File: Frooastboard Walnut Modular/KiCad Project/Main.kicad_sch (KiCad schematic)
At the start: 214 parts, among them J10 F Row CS, J11 F Row SW, J15 F Row, J16 F Row USB, J17 Numpad, J8 Numpad CS, J9 Numpad SW, M2 Frooastboard_MM2040

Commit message: some stuff and caps lock
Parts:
- added MX22: Caps Lock, MX_Only:MXOnly-1U-NoLED, symbol MX_Alps_Hybrid:MX-NoLED
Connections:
- net COL0: now also MX22.1 (COL)
- net at D115.2 (A), MX41.2 (ROW): now also MX22.2 (ROW)
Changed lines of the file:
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@@
   (junction (at 223.52 72.39) (diameter 0) (color 0 0 0 0)
   )
+  (junction (at 58.42 222.25) (diameter 0) (color 0 0 0 0)
+  )
   (junction (at 172.72 195.58) (diameter 0) (color 0 0 0 0)
   )
@@
   (junction (at 256.54 40.64) (diameter 0) (color 0 0 0 0)
   )
+  (junction (at 63.5 217.17) (diameter 0) (color 0 0 0 0)
+  )
   (junction (at 63.5 54.61) (diameter 0) (color 0 0 0 0)
   )
@@
         )
       )
+    )
+  )
+  (symbol (lib_id "MX_Alps_Hybrid:MX-NoLED") (at 59.69 218.44 0) (unit 1)
+    (in_bom yes) (on_board yes) (dnp no) (fields_autoplaced)
+    (property "Reference" "MX22" (at 60.5756 212.09 0)
+      (effects (font (size 1.524 1.524)))
+    )
+    (property "Value" "Caps Lock" (at 60.5756 213.36 0)
+      (effects (font (size 0.508 0.508)))
+    )
+    (property "Footprint" "MX_Only:MXOnly-1U-NoLED" (at 43.815 219.075 0)
+      (effects (font (size 1.524 1.524)) hide)
+    )
+    (property "Datasheet" "" (at 43.815 219.075 0)
+      (effects (font (size 1.524 1.524)) hide)
+    )
+    (pin "1")
+    (pin "2")
+    (instances
+      (project "Frooastboard Walnut Modular"
+        (path "/e63e39d7-6ac0-4ffd-8aa3-1841a4541b55/da496a6d-9c73-4726-8a69-2d6a4df38c58"
+          (reference "MX22") (unit 1)
+        )
+      )

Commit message: stuff
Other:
- moved on the sheet: MX42
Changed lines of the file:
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@@
   (junction (at 177.8 54.61) (diameter 0) (color 0 0 0 0)
   )
-  (junction (at 58.42 238.76) (diameter 0) (color 0 0 0 0)
-  )
   (junction (at 325.12 58.42) (diameter 0) (color 0 0 0 0)
   )
@@
   (junction (at 119.38 58.42) (diameter 0) (color 0 0 0 0)
   )
-  (junction (at 63.5 233.68) (diameter 0) (color 0 0 0 0)
-  )
   (junction (at 162.56 231.14) (diameter 0) (color 0 0 0 0)
   )
@@
   (junction (at 38.1 91.44) (diameter 0) (color 0 0 0 0)
   )
+  (junction (at 58.42 238.76) (diameter 0) (color 0 0 0 0)
+  )
   (junction (at 267.97 138.43) (diameter 0) (color 0 0 0 0)
   )
@@
   (junction (at 335.28 55.88) (diameter 0) (color 0 0 0 0)
   )
+  (junction (at 63.5 233.68) (diameter 0) (color 0 0 0 0)
+  )
   (junction (at 309.88 36.83) (diameter 0) (color 0 0 0 0)
   )
@@
     (stroke (width 0) (type default))
   )
+  (wire (pts (xy 63.5 232.41) (xy 63.5 233.68))
+    (stroke (width 0) (type default))
+  )
   (wire (pts (xy 292.1 72.39) (xy 287.02 72.39))
     (stroke (width 0) (type default))
@@
     (stroke (width 0) (type default))
   )
+  (wire (pts (xy 57.15 238.76) (xy 58.42 238.76))
+    (stroke (width 0) (type default))
+  )
   (wire (pts (xy 25.4 58.42) (xy 50.8 58.42))
     (stroke (width 0) (type default))
@@
     (stroke (width 0) (type default))
   )
+  (wire (pts (xy 62.23 232.41) (xy 63.5 232.41))
+    (stroke (width 0) (type default))
+  )
   (wire (pts (xy 124.46 78.74) (xy 147.32 78.74))
     (stroke (width 0) (type default))
@@
     (stroke (width 0) (type default))
   )
+  (wire (pts (xy 57.15 237.49) (xy 57.15 238.76))
+    (stroke (width 0) (type default))
+  )
   (wire (pts (xy 396.24 173.99) (xy 396.24 176.53))
     (stroke (width 0) (type default))
@@
     )
   )
-  (symbol (lib_id "MX_Alps_Hybrid:MX-NoLED") (at 59.69 234.95 0) (unit 1)
+  (symbol (lib_id "MX_Alps_Hybrid:MX-NoLED") (at 58.42 233.68 0) (unit 1)
     (in_bom yes) (on_board yes) (dnp no) (fields_autoplaced)
-    (property "Reference" "MX42" (at 60.5756 228.6 0)
+    (property "Reference" "MX42" (at 59.3056 227.33 0)
       (effects (font (size 1.524 1.524)))
     )
-    (property "Value" "Left Shift" (at 60.5756 229.87 0)
+    (property "Value" "Left Shift" (at 59.3056 228.6 0)
       (effects (font (size 0.508 0.508)))
     )
-    (property "Footprint" "MX_Only:MXOnly-1.25U-NoLED" (at 43.815 235.585 0)
+    (property "Footprint" "MX_Only:MXOnly-1.25U-NoLED" (at 42.545 234.315 0)
       (effects (font (size 1.524 1.524)) hide)
     )
-    (property "Datasheet" "" (at 43.815 235.585 0)
+    (property "Datasheet" "" (at 42.545 234.315 0)
       (effects (font (size 1.524 1.524)) hide)
     )

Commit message: all keys placed
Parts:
- added MX114: Super Delete, MX_Only:MXOnly-1U-NoLED, symbol MX_Alps_Hybrid:MX-NoLED
- added MX115: End, MX_Only:MXOnly-1U-NoLED, symbol MX_Alps_Hybrid:MX-NoLED
- added MX116: Home, MX_Only:MXOnly-1U-NoLED, symbol MX_Alps_Hybrid:MX-NoLED
- added MX117: Right Control, MX_Only:MXOnly-1U-NoLED, symbol MX_Alps_Hybrid:MX-NoLED
- added MX118: Menu, MX_Only:MXOnly-1U-NoLED, symbol MX_Alps_Hybrid:MX-NoLED
- added MX119: Right Alt, MX_Only:MXOnly-1U-NoLED, symbol MX_Alps_Hybrid:MX-NoLED
- added MX120: Function, MX_Only:MXOnly-1U-NoLED, symbol MX_Alps_Hybrid:MX-NoLED
- added MX121: Shifted Function, MX_Only:MXOnly-1U-NoLED, symbol MX_Alps_Hybrid:MX-NoLED
- added MX122: Space TS, MX_Only:MXOnly-7U-ReversedStabilizers-NoLED, symbol MX_Alps_Hybrid:MX-NoLED
- added MX123: Left Control TS, MX_Only:MXOnly-1.5U-NoLED, symbol MX_Alps_Hybrid:MX-NoLED
- added MX124: Left GUI TS, MX_Only:MXOnly-1U-NoLED, symbol MX_Alps_Hybrid:MX-NoLED
- added MX125: Left Alt TS, MX_Only:MXOnly-1.5U-NoLED, symbol MX_Alps_Hybrid:MX-NoLED
- added MX126: Super Function, MX_Only:MXOnly-1U-NoLED, symbol MX_Alps_Hybrid:MX-NoLED
- added MX127: Right Alt TS, MX_Only:MXOnly-1.5U-NoLED, symbol MX_Alps_Hybrid:MX-NoLED
- added MX128: Backspace, MX_Only:MXOnly-1U-NoLED, symbol MX_Alps_Hybrid:MX-NoLED
- added MX129: Menu TS, MX_Only:MXOnly-1U-NoLED, symbol MX_Alps_Hybrid:MX-NoLED
- added MX130: Right Control TS, MX_Only:MXOnly-1.5U-NoLED, symbol MX_Alps_Hybrid:MX-NoLED
- added MX27: Page Down, MX_Only:MXOnly-1U-NoLED, symbol MX_Alps_Hybrid:MX-NoLED
- added MX33: Page Up, MX_Only:MXOnly-1U-NoLED, symbol MX_Alps_Hybrid:MX-NoLED
- added MX36: Right Shift, MX_Only:MXOnly-1.75U-NoLED, symbol MX_Alps_Hybrid:MX-NoLED
- added MX38: Left, MX_Only:MXOnly-1U-NoLED, symbol MX_Alps_Hybrid:MX-NoLED
- MX90: footprint MX_Only:MXOnly-ISO-ROTATED-NoLED-NoStabilizers -> MX_Only:MXOnly-ISO-ROTATED-NoLED
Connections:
- net COL0: now also MX123.1 (COL)
- net COL1: now also MX124.1 (COL)
- net COL2: now also MX125.1 (COL)
- net COL3: now also MX122.1 (COL)
- net COL4: now also MX119.1 (COL), MX127.1 (COL), MX36.1 (COL)
- net COL5: now also MX120.1 (COL), MX128.1 (COL)
- net COL6: now also MX115.1 (COL), MX116.1 (COL), MX118.1 (COL), MX129.1 (COL), MX38.1 (COL)
- net COL7: now also MX117.1 (COL), MX130.1 (COL), MX27.1 (COL), MX33.1 (COL)
- net at D183.2 (A), MX89.2 (ROW): now also MX128.2 (ROW)
- net at D191.2 (A), MX97.2 (ROW): now also MX118.2 (ROW), MX129.2 (ROW)
- net at D169.2 (A), MX79.2 (ROW): now also MX119.2 (ROW), MX127.2 (ROW)
- net at D117.2 (A), MX43.2 (ROW): now also MX123.2 (ROW)
- net at D203.2 (A), MX106.2 (ROW): now also MX117.2 (ROW), MX130.2 (ROW)
- net at D195.2 (A), MX98.2 (ROW): now also MX38.2 (ROW)
- net at D173.2 (A), MX83.2 (ROW): now also MX36.2 (ROW)
- net at D198.2 (A), MX101.2 (ROW): now also MX115.2 (ROW)
- net at D206.2 (A), MX109.2 (ROW): now also MX33.2 (ROW)
- net at D143.2 (A), MX61.2 (ROW): now also MX125.2 (ROW)
- net at D197.2 (A), MX100.2 (ROW): now also MX116.2 (ROW)
- net at D178.2 (A), MX88.2 (ROW): now also MX120.2 (ROW)
- net at D156.2 (A), MX70.2 (ROW): now also MX122.2 (ROW)
- net at D130.2 (A), MX52.2 (ROW): now also MX124.2 (ROW)
- net at D207.2 (A), MX110.2 (ROW): now also MX27.2 (ROW)
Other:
- moved on the sheet: D113, D114, D115, D116, D117, D122, D123, D124, D125, D126, D127, D128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

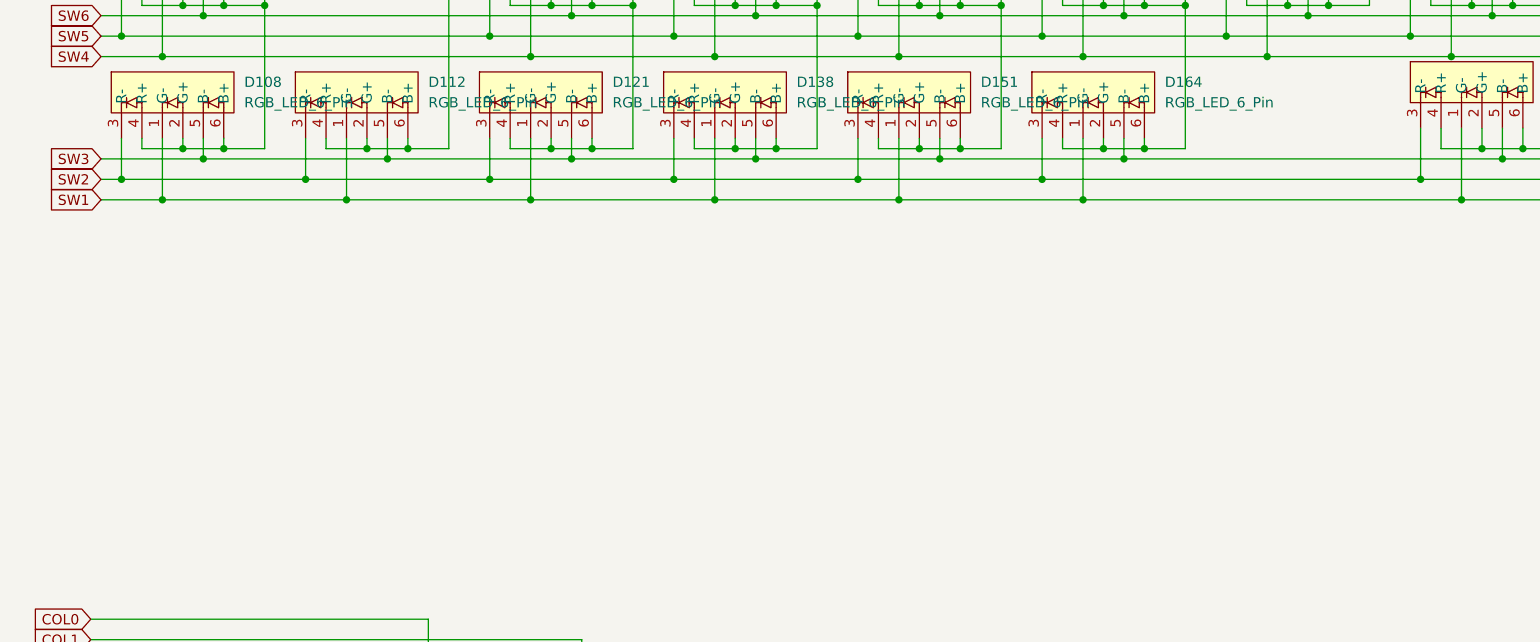
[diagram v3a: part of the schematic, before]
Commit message: some leds and stuff
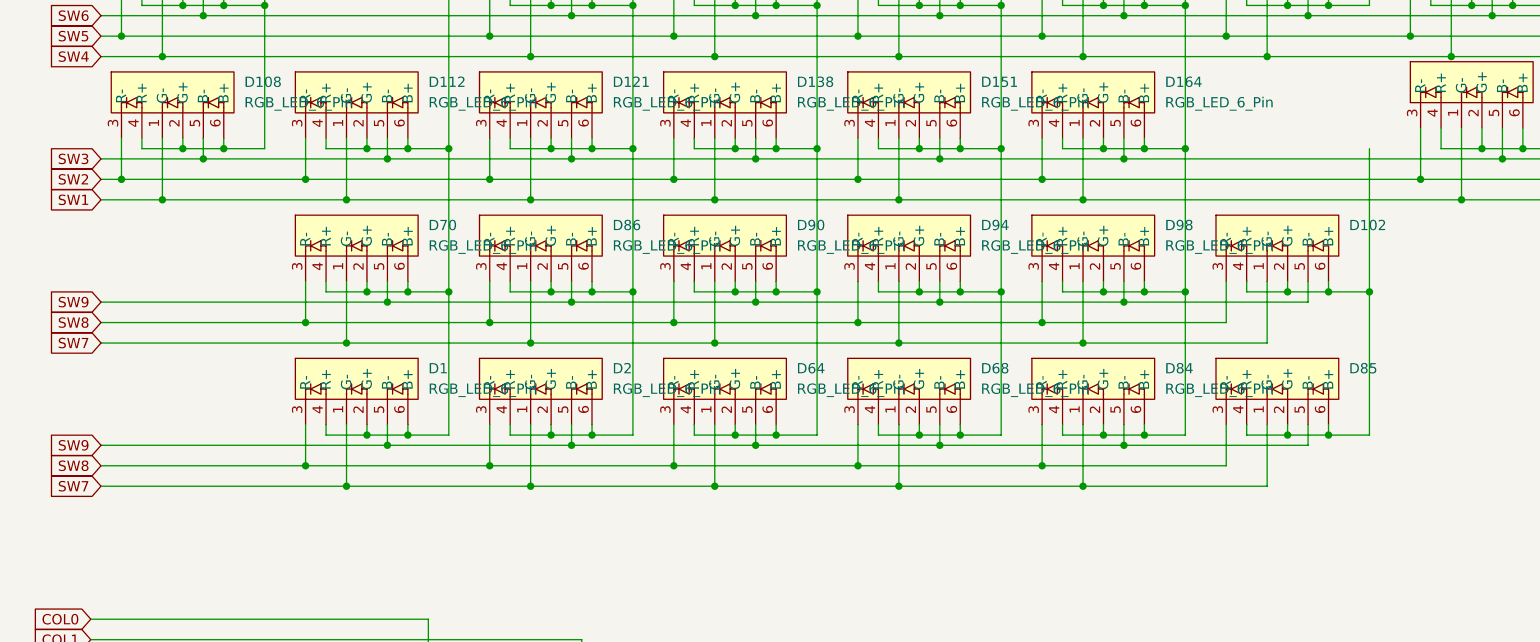
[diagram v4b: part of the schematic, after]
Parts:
- added D1, D102, D2, D64, D68, D70, D84, D85, D86, D90, D94, D98: RGB_LED_6_Pin, Frooastboard Footprints:Everlight 99-235, symbol Frooastboard Symbols:RGB_LED_6_Pin
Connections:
- net CS2: now also D1.2 (G+), D1.4 (R+), D1.6 (B+), D70.2 (G+), D70.4 (R+), D70.6 (B+)
- net CS3: now also D2.2 (G+), D2.4 (R+), D2.6 (B+), D86.2 (G+), D86.4 (R+), D86.6 (B+)
- net CS4: now also D64.2 (G+), D64.4 (R+), D64.6 (B+), D90.2 (G+), D90.4 (R+), D90.6 (B+)
- net CS5: now also D68.2 (G+), D68.4 (R+), D68.6 (B+), D94.2 (G+), D94.4 (R+), D94.6 (B+)
- net CS6: now also D84.2 (G+), D84.4 (R+), D84.6 (B+), D98.2 (G+), D98.4 (R+), D98.6 (B+)
- net SW7: now also D1.1 (G-), D102.1 (G-), D2.1 (G-), D64.1 (G-), D68.1 (G-), D70.1 (G-), D84.1 (G-), D85.1 (G-), D86.1 (G-), D90.1 (G-), D94.1 (G-), D98.1 (G-)
- net SW8: now also D1.3 (R-), D102.3 (R-), D2.3 (R-), D64.3 (R-), D68.3 (R-), D70.3 (R-), D84.3 (R-), D85.3 (R-), D86.3 (R-), D90.3 (R-), D94.3 (R-), D98.3 (R-)
- net SW9: now also D1.5 (B-), D102.5 (B-), D2.5 (B-), D64.5 (B-), D68.5 (B-), D70.5 (B-), D84.5 (B-), D85.5 (B-), D86.5 (B-), D90.5 (B-), D94.5 (B-), D98.5 (B-)
- new net: D102.2 (G+), D102.4 (R+), D102.6 (B+), D85.2 (G+), D85.4 (R+), D85.6 (B+)

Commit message: fix some issues
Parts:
- added D87, D88, D89: D_Small, Diode_SMD:D_0805_2012Metric, symbol Device:D_Small
- J10: symbol Connector:Conn_01x16_Female -> Connector:Conn_01x16_Socket
- J11, J9: symbol Connector:Conn_01x06_Female -> Connector:Conn_01x06_Socket
- J15: symbol Connector:Conn_01x10_Female -> Connector:Conn_01x10_Socket
- J16: symbol Connector:Conn_01x04_Female -> Connector:Conn_01x04_Socket
- J17: symbol Connector:Conn_01x13_Female -> Connector:Conn_01x13_Socket
- J8: symbol Connector:Conn_01x15_Female -> Connector:Conn_01x15_Socket
- MX22: footprint MX_Only:MXOnly-1U-NoLED -> MX_Only:MXOnly-1U; symbol MX_Alps_Hybrid:MX-NoLED -> MX_Alps_Hybrid:MX-LED
- MX41: symbol MX_Alps_Hybrid:MX-NoLED -> MX_Alps_Hybrid:MX-LED
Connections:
- net COL0: now also MX114.1 (COL)
- net COL1: now also MX121.1 (COL)
- net COL2: now also MX126.1 (COL)
- net CS2: now also MX22.3 (LED), MX41.3 (LED)
- net ROW11: now also D87.1 (K), D88.1 (K), D89.1 (K)
- net SW4: now also MX22.4 (LEDGND), MX41.4 (LEDGND)
- net at MX126.2 (ROW): now also D89.2 (A)
- net at MX114.2 (ROW): now also D87.2 (A)
- net at MX121.2 (ROW): now also D88.2 (A)
- no-connect marks 2 -> 4

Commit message: actually place leds good
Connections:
- net CS2: no longer D112.2 (G+), D112.4 (R+), D112.6 (B+)
- net CS3: no longer D120.2 (G+), D120.4 (R+), D120.6 (B+), D121.2 (G+), D121.4 (R+), D121.6 (B+)
- net CS4: no longer D137.2 (G+), D137.4 (R+), D137.6 (B+), D138.2 (G+), D138.4 (R+), D138.6 (B+)
- net CS5: no longer D150.2 (G+), D150.4 (R+), D150.6 (B+), D151.2 (G+), D151.4 (R+), D151.6 (B+)
- net CS6: no longer D163.2 (G+), D163.4 (R+), D163.6 (B+), D164.2 (G+), D164.4 (R+), D164.6 (B+)
- net CS7: now also D102.2 (G+), D102.4 (R+), D102.6 (B+), D85.2 (G+), D85.4 (R+), D85.6 (B+); no longer D181.2 (G+), D181.4 (R+), D181.6 (B+)
- new net: D150.2 (G+), D150.4 (R+), D150.6 (B+), D151.2 (G+), D151.4 (R+), D151.6 (B+)
- new net: D163.2 (G+), D163.4 (R+), D163.6 (B+), D164.2 (G+), D164.4 (R+), D164.6 (B+)
- new net: D120.2 (G+), D120.4 (R+), D120.6 (B+), D121.2 (G+), D121.4 (R+), D121.6 (B+)
- new net: D181.2 (G+), D181.4 (R+), D181.6 (B+)
- new net: D137.2 (G+), D137.4 (R+), D137.6 (B+), D138.2 (G+), D138.4 (R+), D138.6 (B+)
- new net: D112.2 (G+), D112.4 (R+), D112.6 (B+)
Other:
- moved on the sheet: D1, D102, D110, D119, D136, D149, D162, D180, D2, D64, D68, D84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
